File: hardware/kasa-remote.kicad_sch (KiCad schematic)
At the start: 42 parts, among them J1 USB4105-GF-A, J2 S2B-PH-SM4-TB, J3 sh1106_vert, J4 sh1106_horiz, Q1 DMP2045U-7, SW1 RotaryEncoder_Switch, SW10 SW_Push, SW11 SW_Push, SW12 BOOT0, SW2 SW_Push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

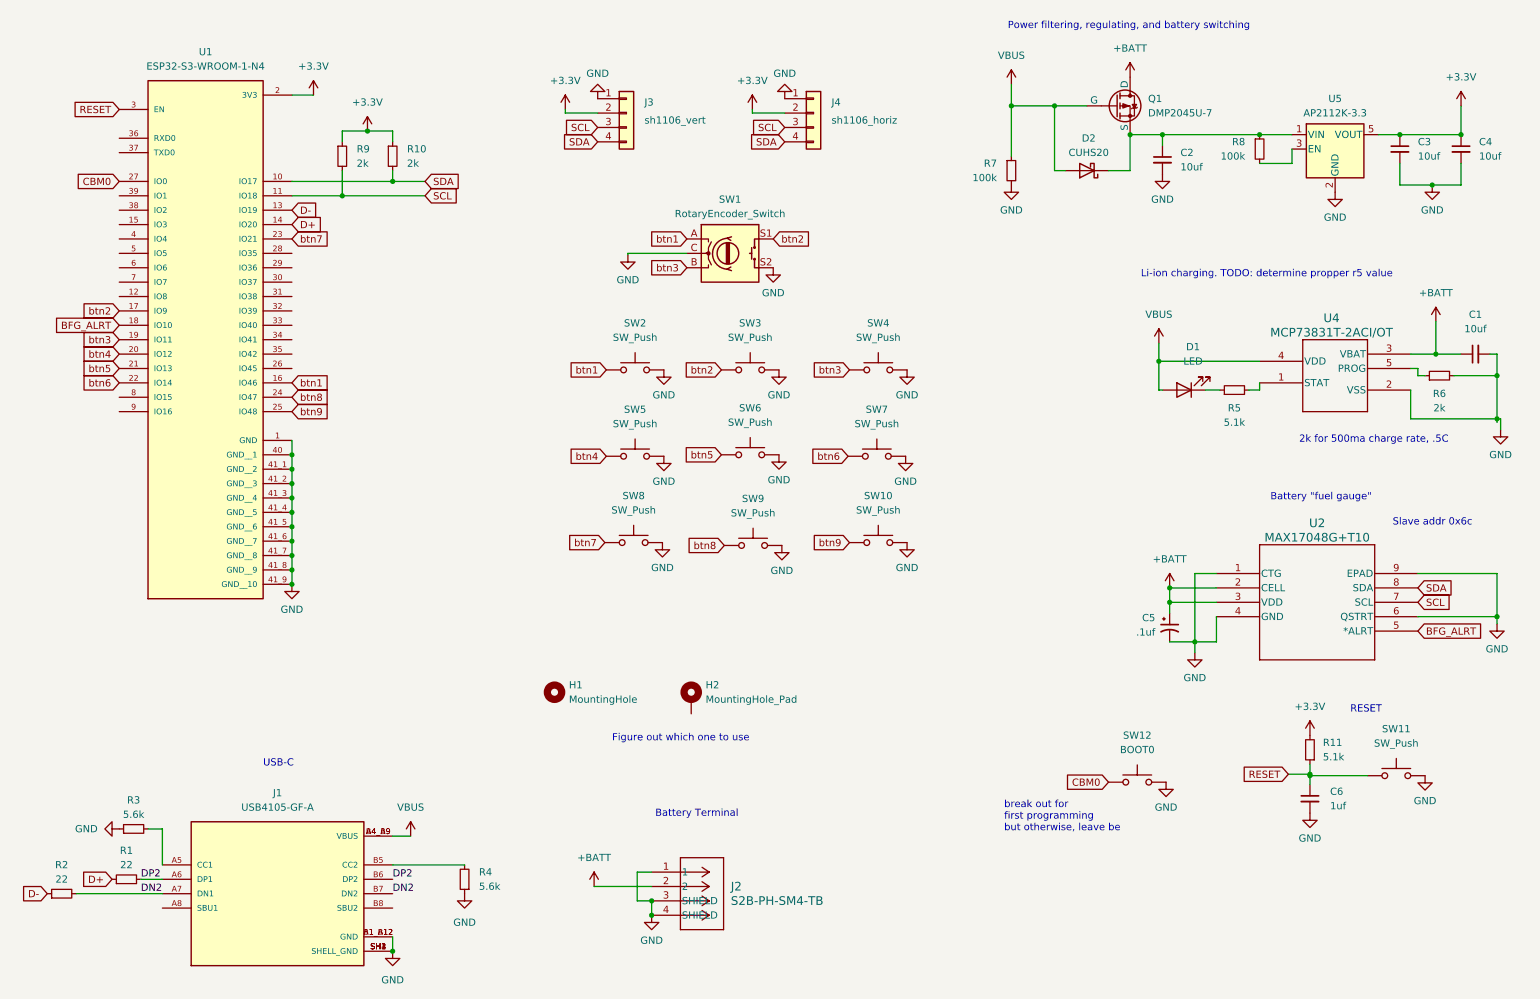
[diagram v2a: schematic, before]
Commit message: layout just about done, no more errors at least
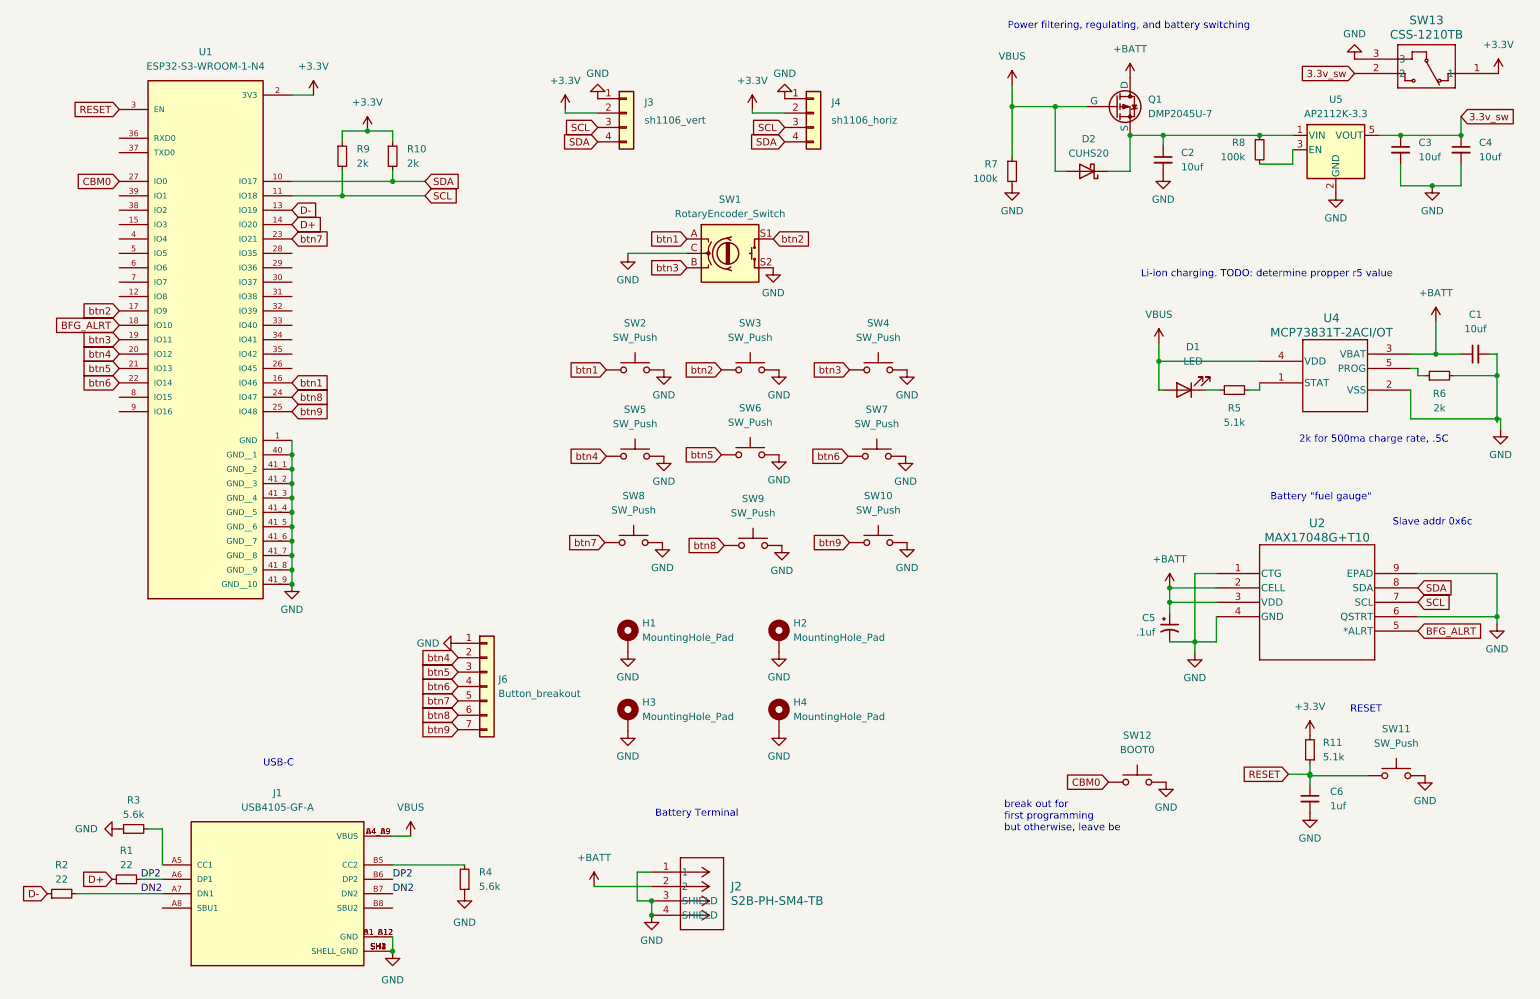
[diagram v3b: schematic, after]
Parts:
- removed H1: MountingHole, symbol Mechanical:MountingHole
- added H1, H3, H4: MountingHole_Pad, MountingHole:MountingHole_2.2mm_M2_DIN965_Pad_TopBottom, symbol Mechanical:MountingHole_Pad
- added J6: Button_breakout, Connector_PinHeader_2.54mm:PinHeader_1x07_P2.54mm_Vertical, symbol Connector_Generic:Conn_01x07
- added SW13: CSS-1210TB, CSS-1210TB:CSS-1210TB_NDC, symbol CSS-1210TB:CSS-1210TB
- H2: footprint (none) -> MountingHole:MountingHole_2.2mm_M2_DIN965_Pad_TopBottom
- U1: footprint ESP32-S3-WROOM-1-N4:XCVR_ESP32-S3-WROOM-1-N4 -> PCM_Espressif:ESP32-S3-WROOM-1
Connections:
- net +3.3V: now also SW13.1; no longer C3.1, C4.1, U5.5 (VOUT)
- net GND: now also H2.1, H1.1, H3.1, H4.1, J6.1 (Pin_1), SW13.3
- net btn4: now also J6.2 (Pin_2)
- net btn5: now also J6.3 (Pin_3)
- net btn6: now also J6.4 (Pin_4)
- net btn7: now also J6.5 (Pin_5)
- net btn8: now also J6.6 (Pin_6)
- net btn9: now also J6.7 (Pin_7)
- new net 3.3v_sw: C3.1, C4.1, SW13.2, U5.5 (VOUT)
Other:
- note removed: "Figure out which one to use"
- moved on the sheet: H2

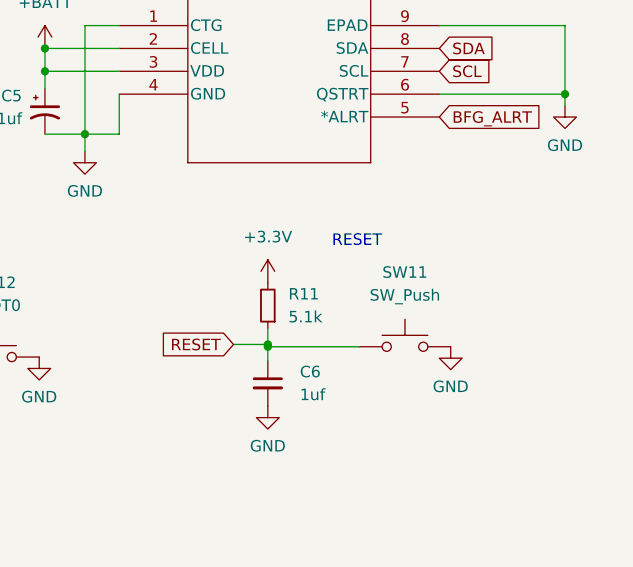
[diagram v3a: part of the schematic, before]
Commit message: added the waywayway for pcb way, also added the bom spreadsheet
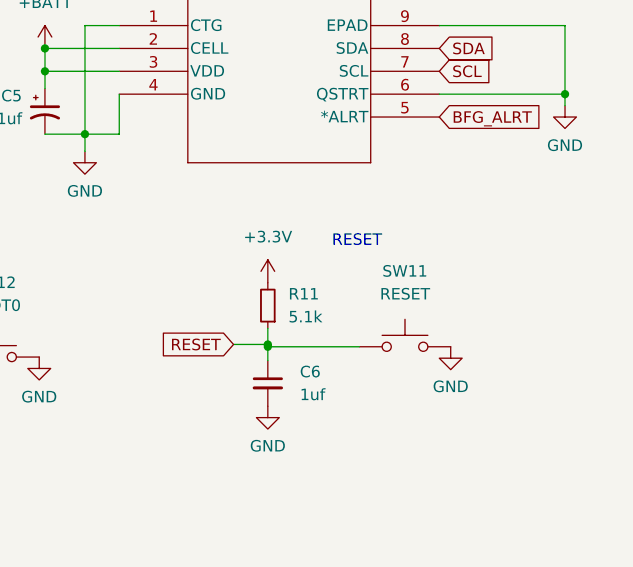
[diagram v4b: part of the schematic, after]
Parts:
- SW11: value SW_Push -> RESET
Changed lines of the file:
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@@
   (symbol (lib_id "Switch:SW_Push") (at 260.35 153.162 0) (unit 1)
     (in_bom yes) (on_board yes) (dnp no) (fields_autoplaced)
-    (property "Reference" "SW11" (at 260.35 144.907 0)
+    (property "Reference" "SW11" (at 260.35 144.78 0)
       (effects (font (size 1.27 1.27)))
     )
-    (property "Value" "SW_Push" (at 260.35 147.447 0)
+    (property "Value" "RESET" (at 260.35 147.32 0)
       (effects (font (size 1.27 1.27)))
     )
